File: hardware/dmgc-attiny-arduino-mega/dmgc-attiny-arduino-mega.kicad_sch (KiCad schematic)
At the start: 28 parts, among them J1 Power, J2 PWM, J3 Analog, J4 PWM, J5 Analog, J6 Communication, J7 Digital, SW1 PUSH, SW2 LEFT, SW3 RIGHT, SW4 SELECT, SW5 START/RESET, U1 ATtiny85-20P

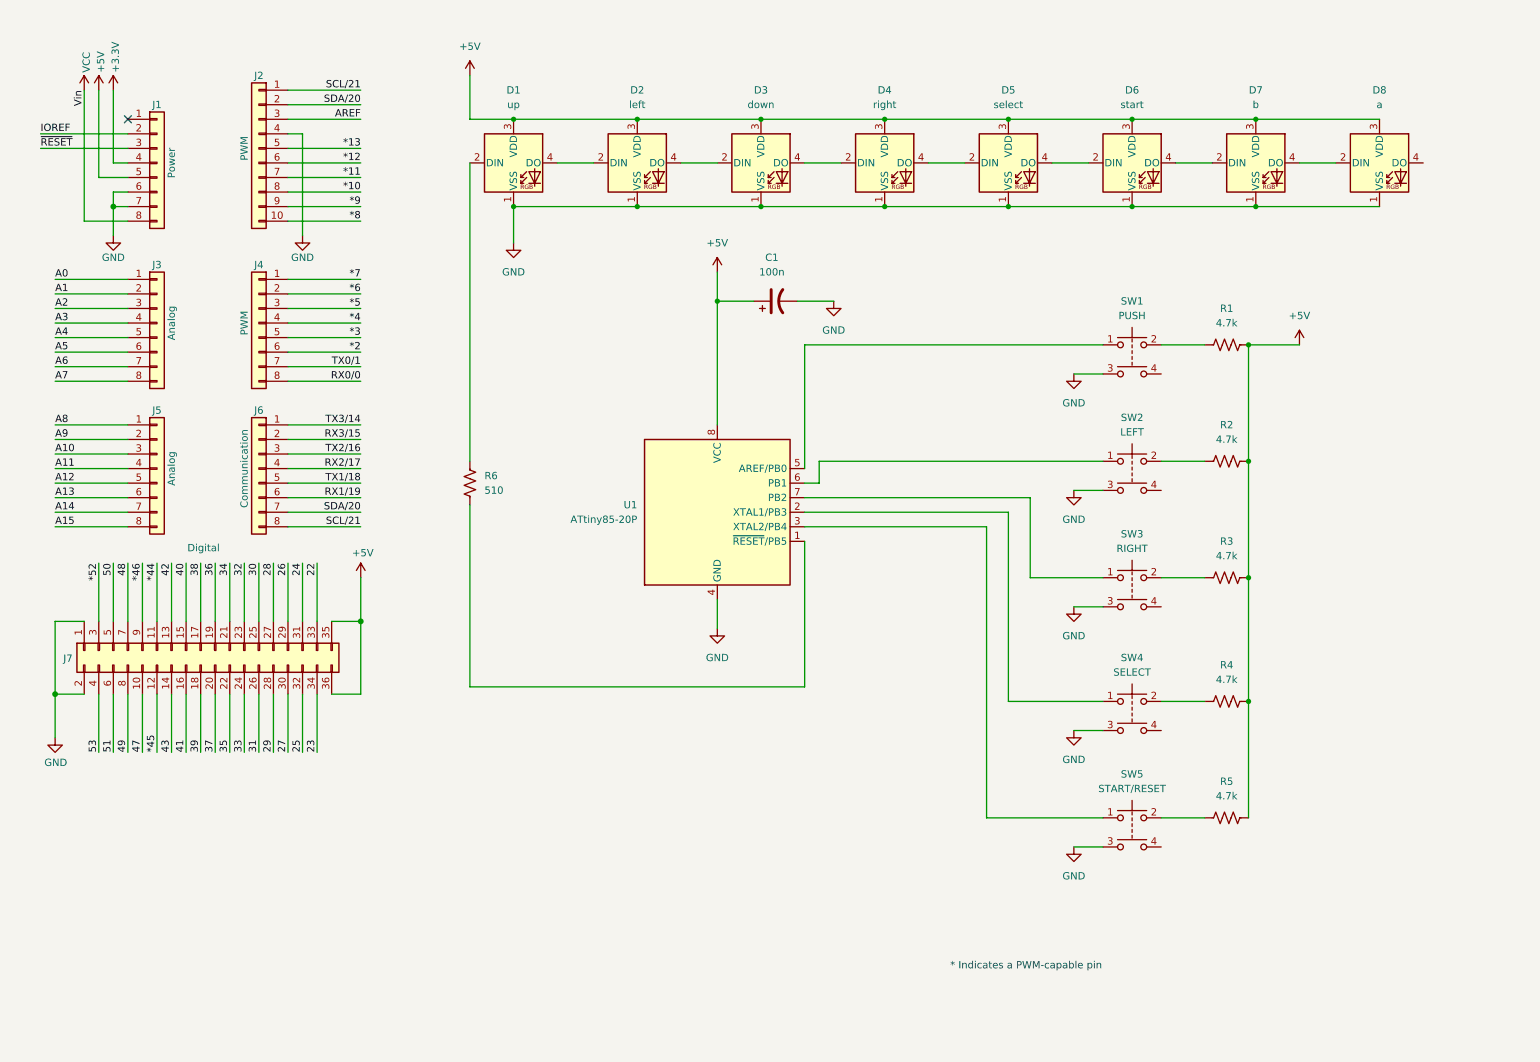
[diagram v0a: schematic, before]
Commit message: Updated arduino shield, start implementing a multiplexer to switch from flashing the attiny85 to running the attiny85.
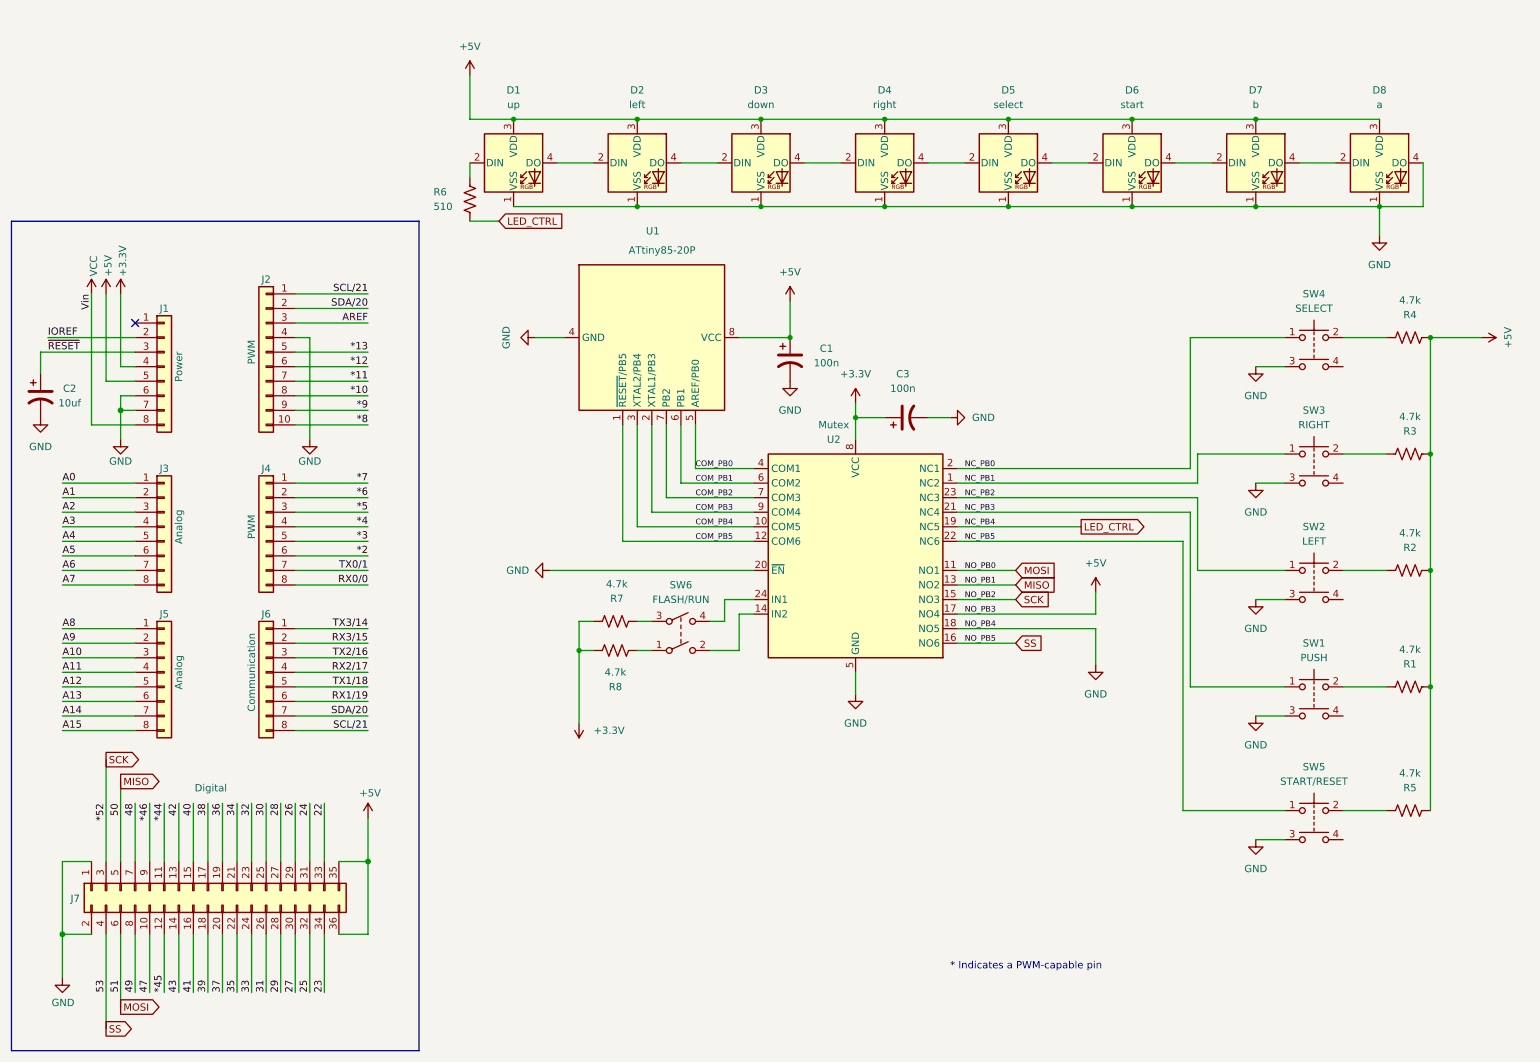
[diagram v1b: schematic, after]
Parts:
- added C2: 10uf, Capacitor_SMD:C_0201_0603Metric, symbol Device:C_Polarized_US
- added C3: 100n, Capacitor_SMD:C_0201_0603Metric, symbol Device:C_Polarized_US
- added R7, R8: 4.7k, Resistor_SMD:R_0201_0603Metric, symbol Device:R_US
- added SW6: FLASH/RUN, symbol Switch:SW_DPST
- added U2: Mutex, Package_SO:TSSOP-24_4.4x7.8mm_P0.65mm, symbol Analog_Switch:TS3A27518EPW
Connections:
- net +5V: now also U2.17 (NO4)
- net GND: now also D8.4 (DO), C2.2, C3.2, U2.18 (NO5), U2.20 (~{EN}), U2.5 (GND)
- net ~{RESET}: now also C2.1
- net COM_PB4: now reaches U1.3 (XTAL2/PB4)
- net COM_PB4: now also U2.10 (COM5); no longer SW5.1
- net at D1.2 (DIN): now also R6.2; no longer R6.1
- net COM_PB5: now reaches U1.1 (~{RESET}/PB5)
- net COM_PB5: now also U2.12 (COM6); no longer R6.2
- net COM_PB0: now reaches U1.5 (AREF/PB0)
- net COM_PB0: now also U2.4 (COM1); no longer SW1.1
- net COM_PB3: now reaches U1.2 (XTAL1/PB3)
- net COM_PB3: now also U2.9 (COM4); no longer SW4.1
- net COM_PB1: now reaches U1.6 (PB1)
- net COM_PB1: now also U2.6 (COM2); no longer SW2.1
- net COM_PB2: now reaches U1.7 (PB2)
- net COM_PB2: now also U2.7 (COM3); no longer SW3.1
- net *52 renamed SCK
- net SCK: now also U2.15 (NO3)
- net 50 renamed MISO
- net MISO: now also U2.13 (NO2)
- net 51 renamed MOSI
- net MOSI: now also U2.11 (NO1)
- net 53 renamed SS
- net SS: now also U2.16 (NO6)
- new net: R7.1, SW6.3
- new net: R8.1, SW6.1
- new net: SW6.2, U2.14 (IN2)
- new net: SW6.4, U2.24 (IN1)
- new net +3.3V: C3.1, R7.2, R8.2, U2.8 (VCC)
- new net LED_CTRL: R6.1, U2.19 (NC5)
- new net NC_PB0: SW4.1, U2.2 (NC1)
- new net NC_PB1: SW3.1, U2.1 (NC2)
- new net NC_PB2: SW2.1, U2.23 (NC3)
- new net NC_PB3: SW1.1, U2.21 (NC4)
- new net NC_PB5: SW5.1, U2.22 (NC6)
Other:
- title: Arduino Mega 2650 DMGC Shield -> DMGC Arduino Mega 2650 Shield
- moved on the sheet: C1, J1, J2, J3, J4, J5, J6, J7, R1, R2, R3, R4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

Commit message: Updated arduino shield to include switching circuit for flashing and running.
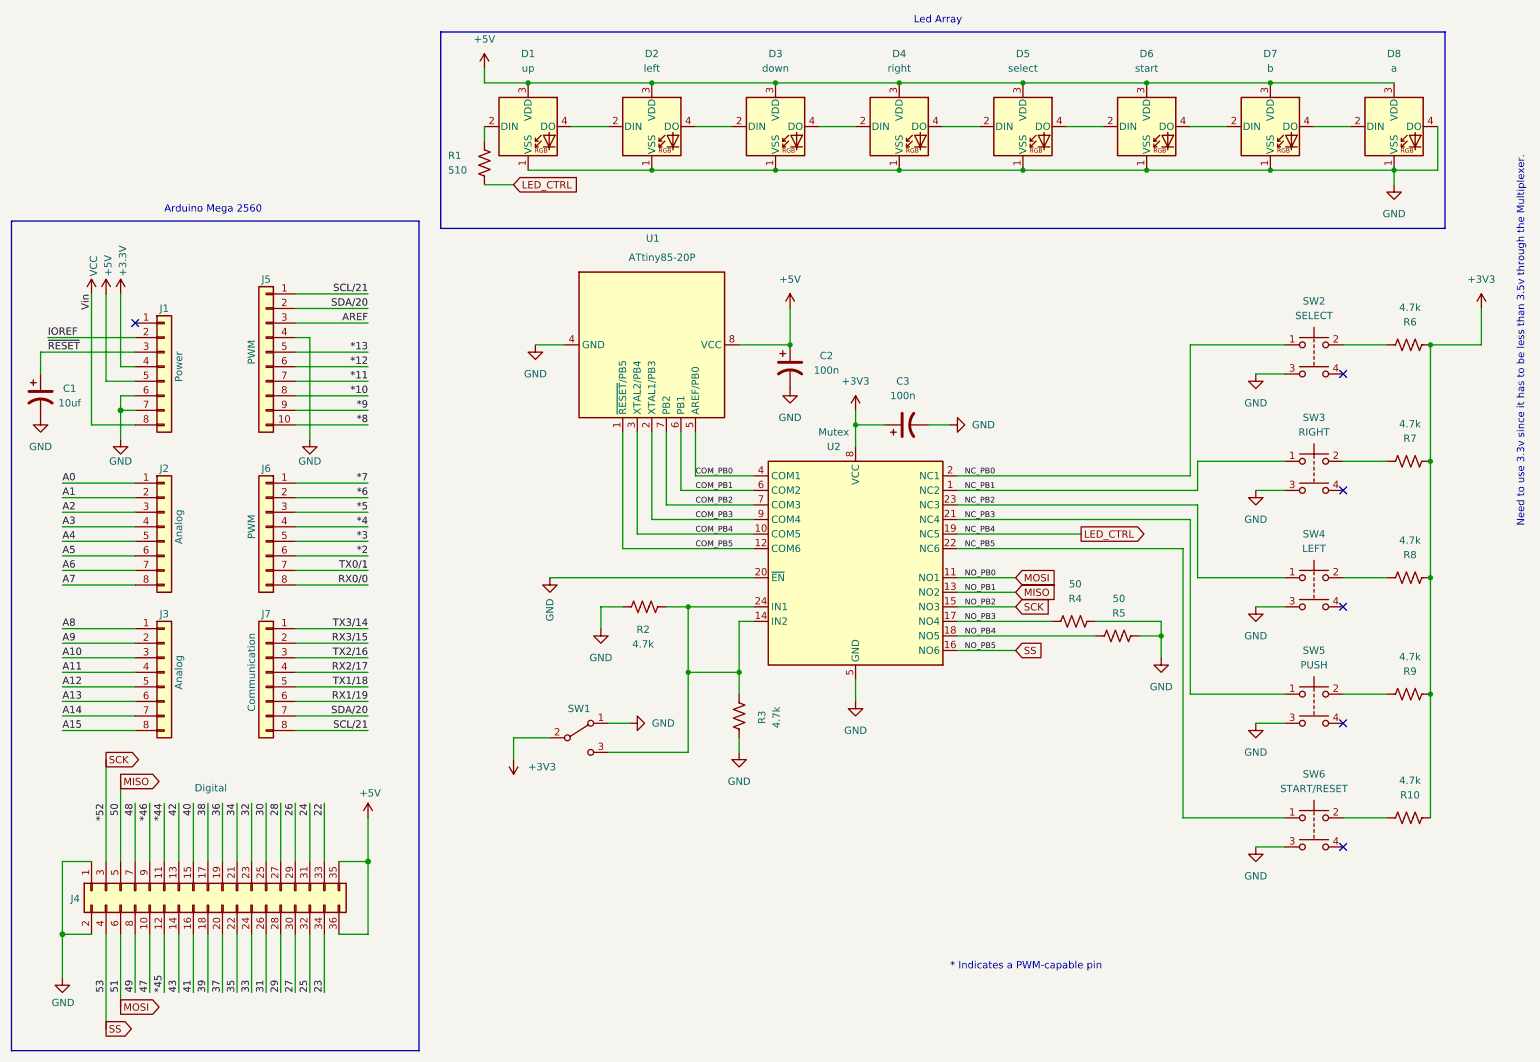
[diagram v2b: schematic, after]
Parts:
- removed R7, R8: 4.7k, Resistor_SMD:R_0201_0603Metric, symbol Device:R_US
- removed SW6: FLASH/RUN, symbol Switch:SW_DPST
- added R2, R3: 4.7k, Resistor_SMD:R_0201_0603Metric, symbol Device:R_US
- added R4, R5: 50, Resistor_SMD:R_0201_0603Metric, symbol Device:R_US
- added SW1: Toggle Flash / Run, Button_Switch_THT:SW_E-Switch_EG1224_SPDT_Angled, symbol Switch:SW_SPDT
- renumbered C2 to C1, C1 to C2, J3 to J2, J5 to J3, J7 to J4, J2 to J5, J4 to J6, J6 to J7, R6 to R1, R5 to R10, R4 to R6, R3 to R7, R2 to R8, R1 to R9, SW4 to SW2, SW2 to SW4, SW1 to SW5, SW5 to SW6
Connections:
- net +3.3V is gone; now on net +3V3: C3.1, U2.8 (VCC)
- net +3V3: now also R10.1, R6.1, R7.1, R8.1, R9.1, SW1.2 (B)
- net +5V: no longer R10.1, R6.1, R7.1, R8.1, R9.1, U2.17 (NO4)
- net GND: now also R2.1, R3.1, R4.1, R5.1, SW1.1 (A); no longer U2.18 (NO5)
- net at U2.14 (IN2): now also U2.24 (IN1), R2.2, R3.2, SW1.3 (C)
- new net NO_PB3: R4.2, U2.17 (NO4)
- new net NO_PB4: R5.2, U2.18 (NO5)
- no-connect marks 1 -> 6
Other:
- note added: "Arduino Mega 2560"
- note added: "Led Array"
- note added: "Need to use 3.3v since it has to be less than 3.5v through the Multiplexer."
- moved on the sheet: C2, C3, D1, D2, D3, D4, D5, D6, D7, D8, R1, R10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

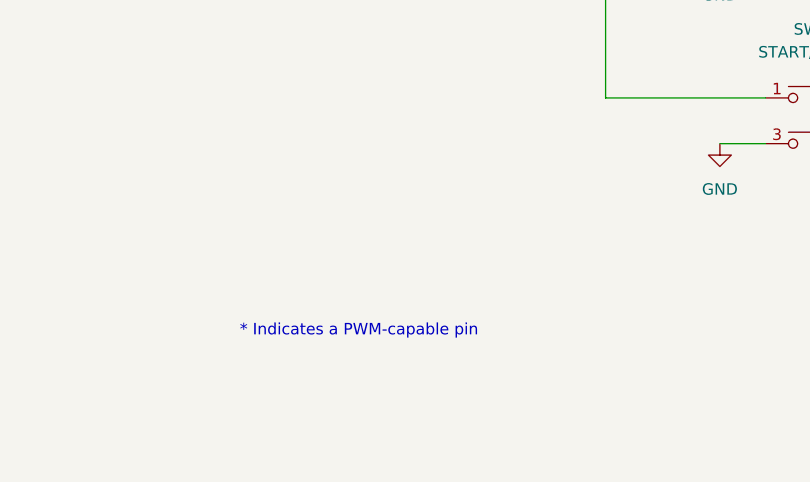
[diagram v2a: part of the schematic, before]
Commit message: Updated arduino shield routing and fixed pcb issues.
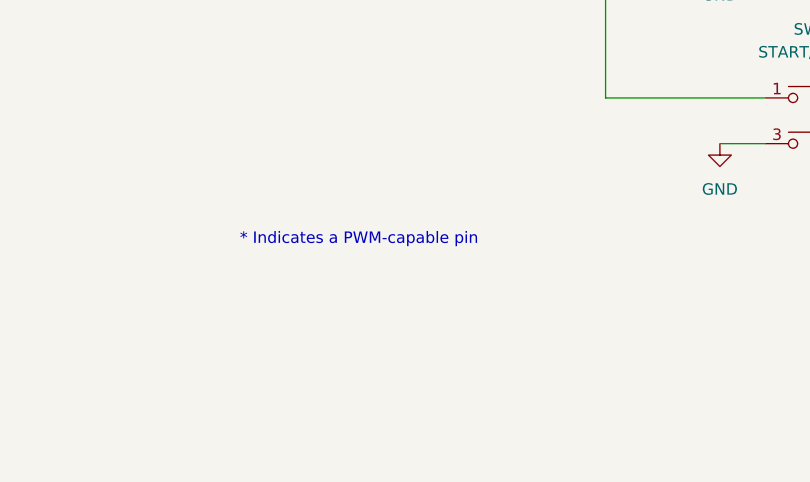
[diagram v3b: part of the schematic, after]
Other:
- company: (none) -> Author: juvinious
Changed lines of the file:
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@@
     (title "DMGC Arduino Mega 2650 Shield")
     (date "mar. 31 mars 2015")
-    (rev "0.1")
+    (rev "0.2")
+    (company "Author: juvinious")
   )
   (junction (at 261.62 111.76) (diameter 0) (color 0 0 0 0)
@@
     (effects (font (size 1.27 1.27)) (justify left bottom))
   )
-  (text "* Indicates a PWM-capable pin" (at 177.8 180.34 0)
+  (text "* Indicates a PWM-capable pin" (at 177.8 170.18 0)
     (effects (font (size 1.27 1.27)) (justify left bottom))
   )
